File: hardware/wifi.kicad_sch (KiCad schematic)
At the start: 33 parts, among them J11 ANT, J7 RJ45_Hanrun_HR913550A_Horizon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, U22 AP6212, U24 AW13412HDNR, Y2 26MHz

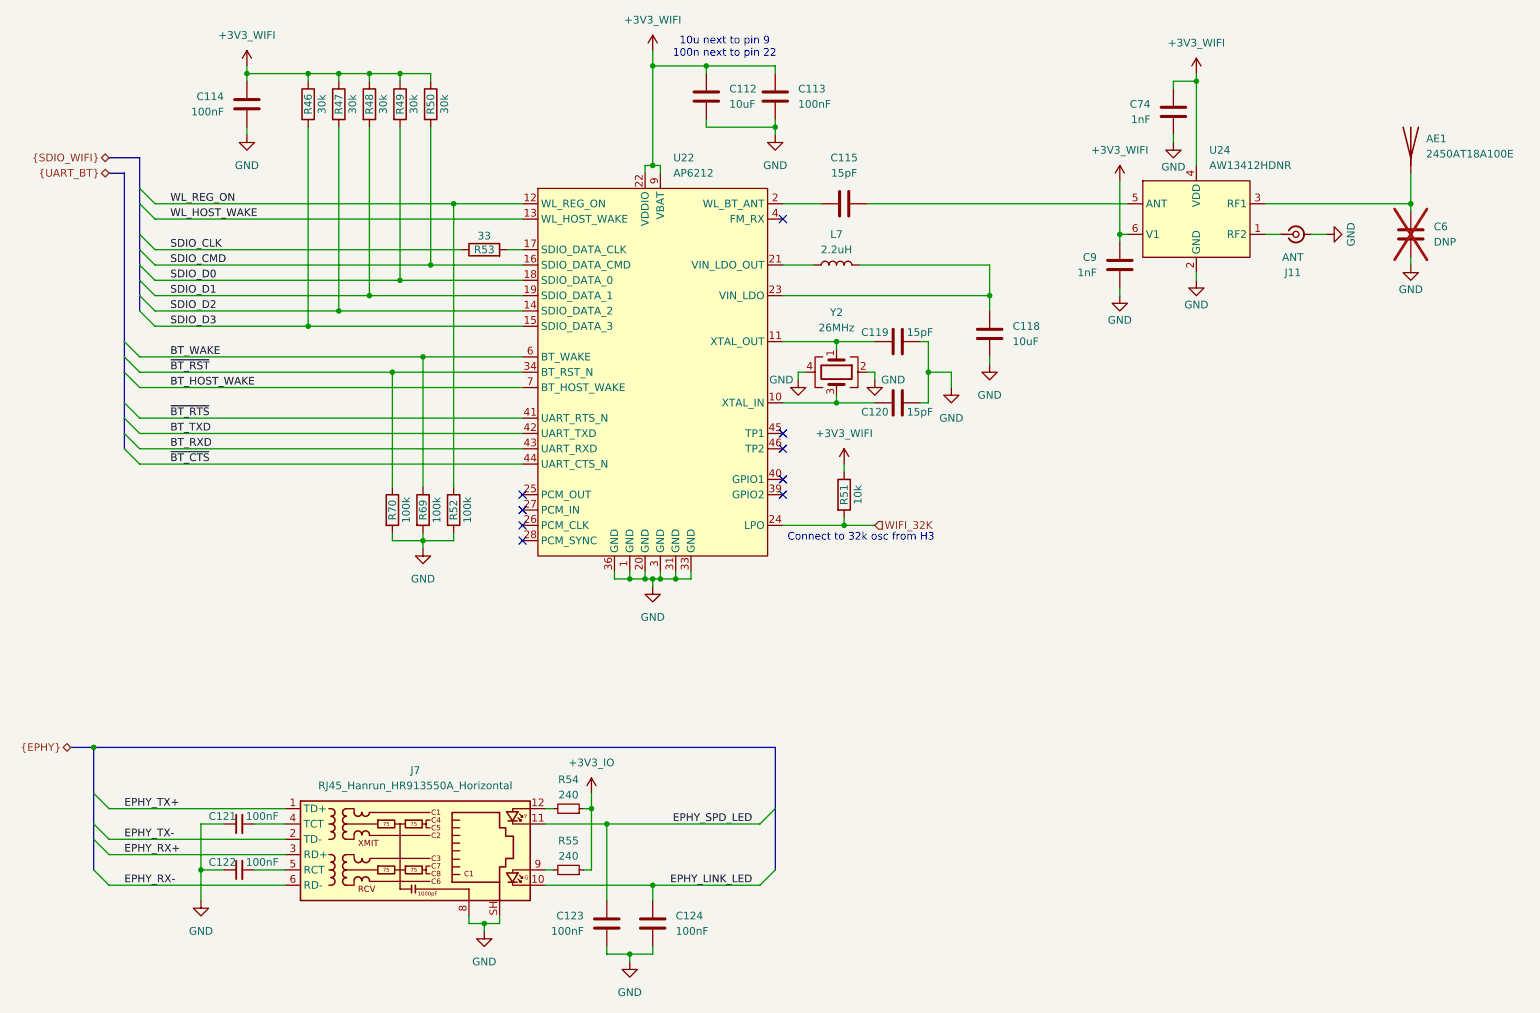
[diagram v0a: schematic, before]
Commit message: Update crystal
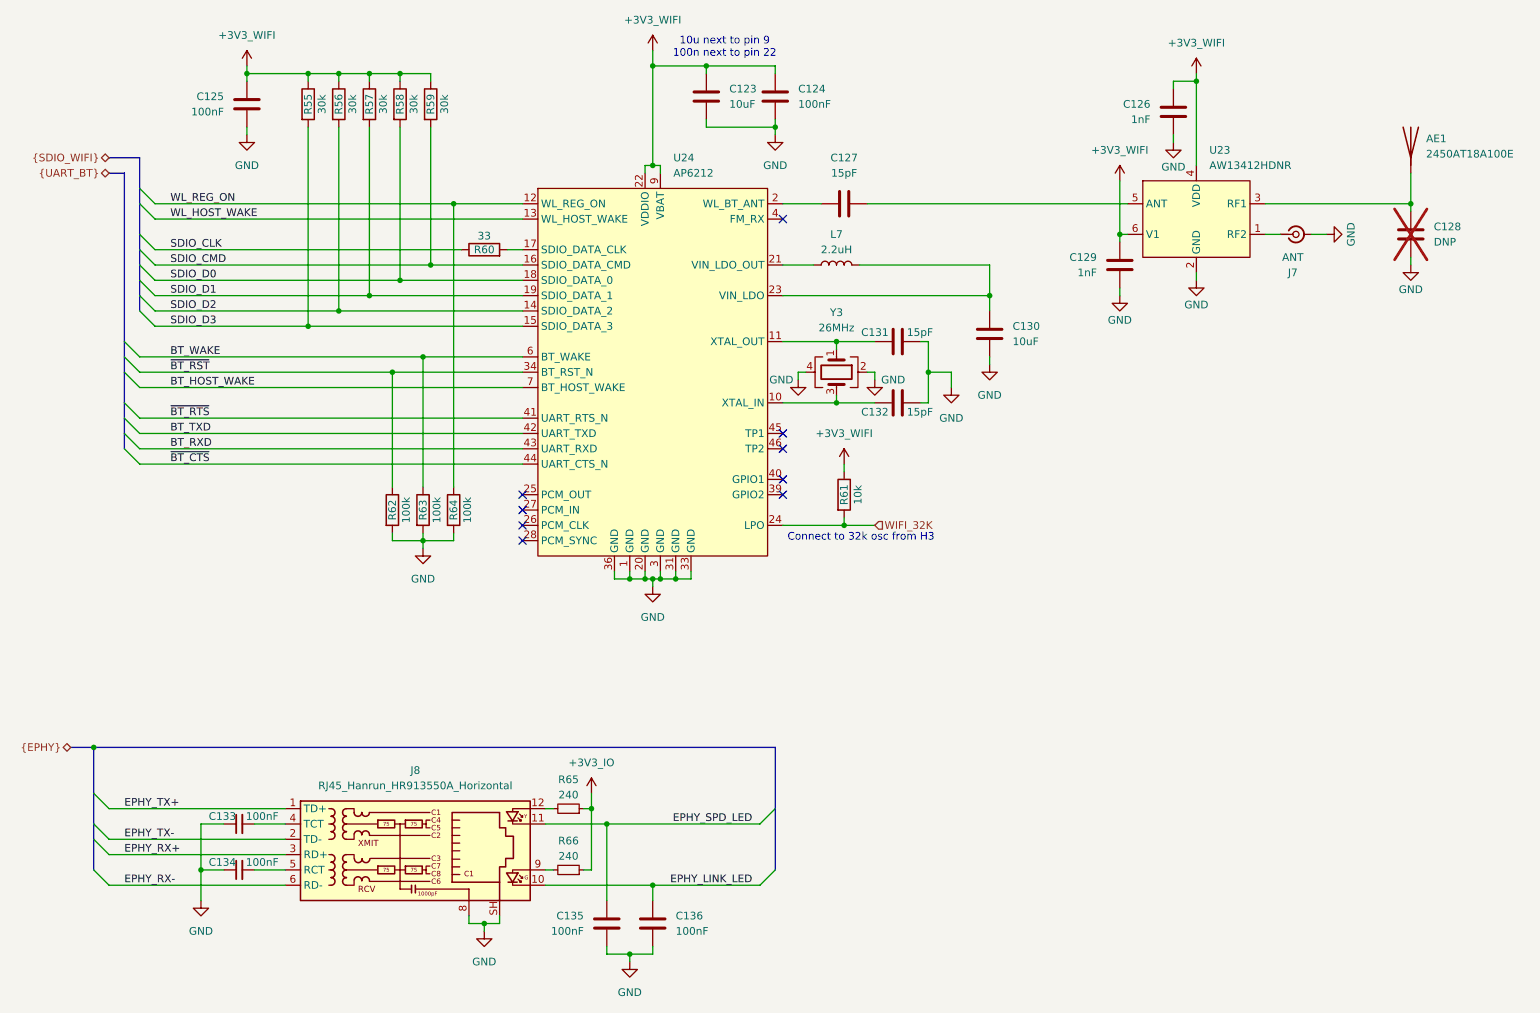
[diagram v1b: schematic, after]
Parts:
- renumbered C112 to C123, C113 to C124, C114 to C125, C74 to C126, C115 to C127, C6 to C128, C9 to C129, C118 to C130, C119 to C131, C120 to C132, C121 to C133, C122 to C134, C123 to C135, C124 to C136, J11 to J7, J7 to J8, R46 to R55, R47 to R56, R48 to R57, R49 to R58, R50 to R59, R53 to R60, R51 to R61, R70 to R62, R69 to R63, R52 to R64, R54 to R65, R55 to R66, U24 to U23, U22 to U24, Y2 to Y3

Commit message: Add schematic pdf
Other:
- title: Icepi CM0 -> Icepi SBC
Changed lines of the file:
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@@
 	(paper "A4")
 	(title_block
-		(title "Icepi CM0")
-		(date "2025-11-21")
+		(title "Icepi SBC")
+		(date "2025-12-21")
 		(rev "v1.0")
 		(company "Icy Electronics")
 		(comment 1 "Chengyin Yao (cheyao)")
-		(comment 2 "https://github.com/cheyao/icepi-cm0")
+		(comment 2 "https://github.com/cheyao/icepi-sbc")
 		(comment 3 "License: Solderpad")
 	)
